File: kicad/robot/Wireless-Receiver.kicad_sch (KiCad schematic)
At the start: 49 parts, among them IC2 STWLC38JRM, J8 Conn_01x02

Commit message: Updated 100uF caps to 1206 footprint to allow for 6.3V ratings
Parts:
- C109, C125, C127, C131, C133, C135, C137, C138: footprint robot:C_0805_2012Metric -> robot:C_1206_3216Metric; Part Number (none) -> GRM31CD80J107MEA8K
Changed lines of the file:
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@@
       (effects (font (size 1.27 1.27)) (justify left))
     )
-    (property "Footprint" "robot:C_0805_2012Metric" (at 157.48 123.4948 0)
+    (property "Footprint" "robot:C_1206_3216Metric" (at 157.48 123.4948 0)
       (effects (font (size 1.27 1.27)) hide)
     )
@@
       (effects (font (size 1.27 1.27)) hide)
     )
-    (property "Part Number" "" (at 161.29 124.46 0)
+    (property "Part Number" "GRM31CD80J107MEA8K" (at 161.29 124.46 0)
       (effects (font (size 1.27 1.27)) hide)
     )
@@
       (effects (font (size 1.27 1.27)) (justify left))
     )
-    (property "Footprint" "robot:C_0805_2012Metric" (at 262.5852 116.84 0)
+    (property "Footprint" "robot:C_1206_3216Metric" (at 262.5852 116.84 0)
       (effects (font (size 1.27 1.27)) hide)
     )
@@
       (effects (font (size 1.27 1.27)) hide)
     )
-    (property "Part Number" "" (at 261.62 120.65 0)
+    (property "Part Number" "GRM31CD80J107MEA8K" (at 261.62 120.65 0)
       (effects (font (size 1.27 1.27)) hide)
     )
@@
       (effects (font (size 1.27 1.27)) (justify left))
     )
-    (property "Footprint" "robot:C_0805_2012Metric" (at 157.48 137.4648 0)
+    (property "Footprint" "robot:C_1206_3216Metric" (at 157.48 137.4648 0)
       (effects (font (size 1.27 1.27)) hide)
     )
@@
       (effects (font (size 1.27 1.27)) hide)
     )
-    (property "Part Number" "" (at 161.29 138.43 0)
+    (property "Part Number" "GRM31CD80J107MEA8K" (at 161.29 138.43 0)
       (effects (font (size 1.27 1.27)) hide)
     )
@@
       (effects (font (size 1.27 1.27)) (justify left))
     )
-    (property "Footprint" "robot:C_0805_2012Metric" (at 223.2152 144.78 0)
+    (property "Footprint" "robot:C_1206_3216Metric" (at 223.2152 144.78 0)
       (effects (font (size 1.27 1.27)) hide)
     )
@@
       (effects (font (size 1.27 1.27)) hide)
     )
-    (property "Part Number" "" (at 222.25 148.59 0)
+    (property "Part Number" "GRM31CD80J107MEA8K" (at 222.25 148.59 0)
       (effects (font (size 1.27 1.27)) hide)
     )
@@
       (effects (font (size 1.27 1.27)) (justify left))
     )
-    (property "Footprint" "robot:C_0805_2012Metric" (at 197.8152 144.78 0)
+    (property "Footprint" "robot:C_1206_3216Metric" (at 197.8152 144.78 0)
       (effects (font (size 1.27 1.27)) hide)
     )
@@
       (effects (font (size 1.27 1.27)) hide)
     )
-    (property "Part Number" "" (at 196.85 148.59 0)
+    (property "Part Number" "GRM31CD80J107MEA8K" (at 196.85 148.59 0)
       (effects (font (size 1.27 1.27)) hide)
     )
@@
       (effects (font (size 1.27 1.27)) (justify left))
     )
-    (property "Footprint" "robot:C_0805_2012Metric" (at 62.5348 125.73 0)
+    (property "Footprint" "robot:C_1206_3216Metric" (at 62.5348 125.73 0)
       (effects (font (size 1.27 1.27)) hide)
     )
@@
       (effects (font (size 1.27 1.27)) hide)
     )
-    (property "Part Number" "" (at 63.5 121.92 0)
+    (property "Part Number" "GRM31CD80J107MEA8K" (at 63.5 121.92 0)
       (effects (font (size 1.27 1.27)) hide)
     )
@@
       (effects (font (size 1.27 1.27)) (justify left))
     )
-    (property "Footprint" "robot:C_0805_2012Metric" (at 247.3452 116.84 0)
+    (property "Footprint" "robot:C_1206_3216Metric" (at 247.3452 116.84 0)
       (effects (font (size 1.27 1.27)) hide)
     )
@@
       (effects (font (size 1.27 1.27)) hide)
     )
-    (property "Part Number" "" (at 246.38 120.65 0)
+    (property "Part Number" "GRM31CD80J107MEA8K" (at 246.38 120.65 0)
       (effects (font (size 1.27 1.27)) hide)
     )
@@
       (effects (font (size 1.27 1.27)) (justify left))
     )
-    (property "Footprint" "robot:C_0805_2012Metric" (at 210.5152 144.78 0)
+    (property "Footprint" "robot:C_1206_3216Metric" (at 210.5152 144.78 0)
       (effects (font (size 1.27 1.27)) hide)
     )
@@
       (effects (font (size 1.27 1.27)) hide)
     )
-    (property "Part Number" "" (at 209.55 148.59 0)
-      (effects (font (size 1.27 1.27)) hide)
-    )
+    (property "Part Number" "GRM31CD80J107MEA8K" (at 209.55 148.59 0)
+      (effects (font (size 1.27 1.27)) hide)
+    )

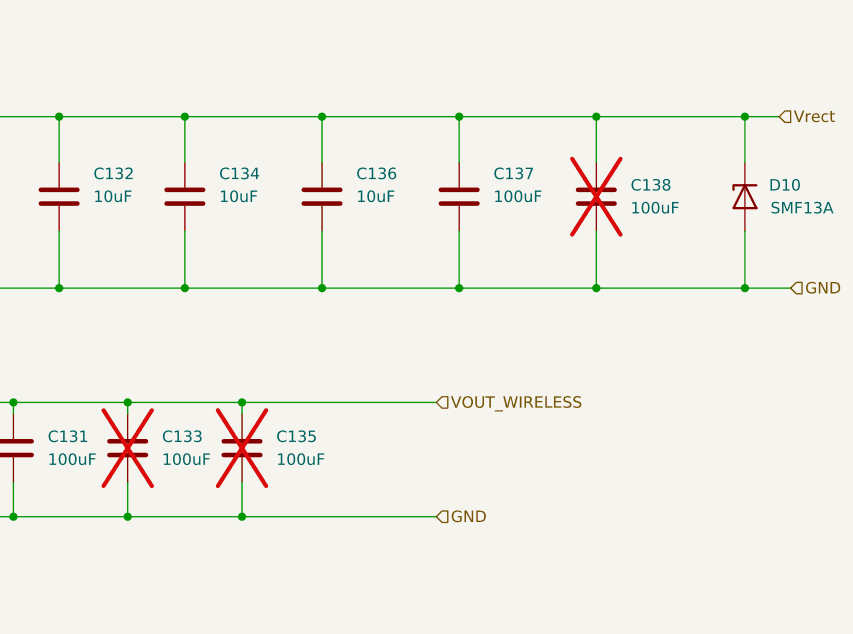
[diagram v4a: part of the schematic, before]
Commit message: Updating wireless 100uF caps to 16V 1210 versions
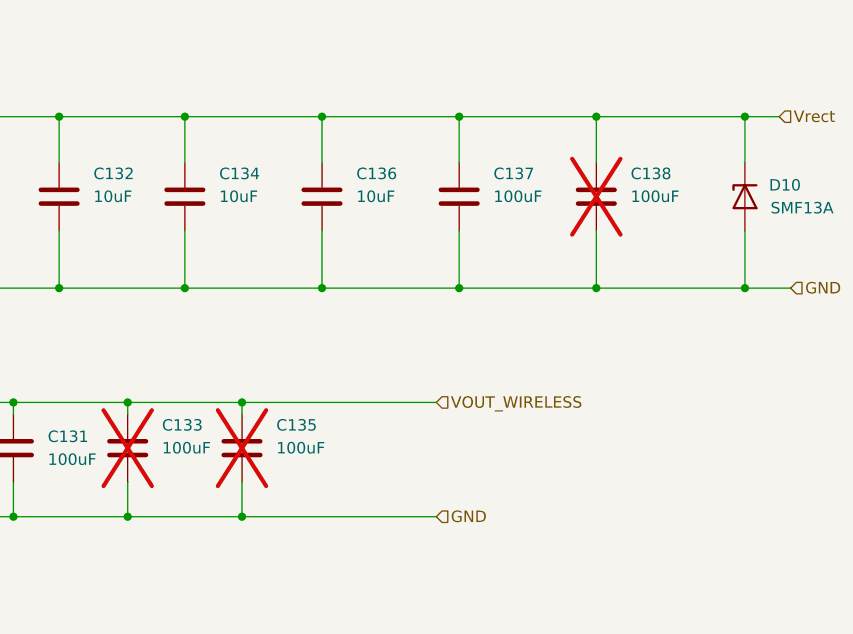
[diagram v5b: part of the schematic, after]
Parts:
- C133, C135, C137, C138: footprint robot:C_1206_3216Metric -> robot:C_1210_3225Metric; Manufacturer Murata -> Cal-Chip Electronics, Inc.; Part Number GRM31CD80J107MEA8K -> GMC32X5R107M16NT; V_Max (none) -> 16V
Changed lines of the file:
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@@
+    )
+  )
+  (symbol (lib_id "robot:C") (at 261.62 120.65 0) (mirror x) (unit 1)
+    (in_bom yes) (on_board yes) (dnp yes)
+    (property "Reference" "C138" (at 265.43 118.11 0)
+      (effects (font (size 1.27 1.27)) (justify left))
+    )
+    (property "Value" "100uF" (at 265.43 120.65 0)
+      (effects (font (size 1.27 1.27)) (justify left))
+    )
+    (property "Footprint" "robot:C_1210_3225Metric" (at 262.5852 116.84 0)
+      (effects (font (size 1.27 1.27)) hide)
+    )
+    (property "Datasheet" "~" (at 261.62 120.65 0)
+      (effects (font (size 1.27 1.27)) hide)
+    )
+    (property "Manufacturer" "Cal-Chip Electronics, Inc." (at 261.62 120.65 0)
+      (effects (font (size 1.27 1.27)) hide)
+    )
+    (property "Part Number" "GMC32X5R107M16NT" (at 261.62 120.65 0)
+      (effects (font (size 1.27 1.27)) hide)
+    )
+    (property "V_Max" "16V" (at 261.62 120.65 0)
+      (effects (font (size 1.27 1.27)) hide)
+    )
+    (pin "1")
+    (pin "2")
+    (instances
+      (project "robot"
+        (path "/0c7b298e-2d07-4b1f-b033-e95f02d45089/d5c9d5c0-7de4-474c-9ba2-6b466f104c70"
+          (reference "C138") (unit 1)
+        )
+      )
     )
   )
@@
     )
   )
-  (symbol (lib_id "robot:C") (at 261.62 120.65 0) (mirror x) (unit 1)
-    (in_bom yes) (on_board yes) (dnp yes)
-    (property "Reference" "C138" (at 265.43 119.38 0)
-      (effects (font (size 1.27 1.27)) (justify left))
-    )
-    (property "Value" "100uF" (at 265.43 121.92 0)
-      (effects (font (size 1.27 1.27)) (justify left))
-    )
-    (property "Footprint" "robot:C_1206_3216Metric" (at 262.5852 116.84 0)
-      (effects (font (size 1.27 1.27)) hide)
-    )
-    (property "Datasheet" "~" (at 261.62 120.65 0)
-      (effects (font (size 1.27 1.27)) hide)
-    )
-    (property "Manufacturer" "Murata" (at 261.62 120.65 0)
-      (effects (font (size 1.27 1.27)) hide)
-    )
-    (property "Part Number" "GRM31CD80J107MEA8K" (at 261.62 120.65 0)
-      (effects (font (size 1.27 1.27)) hide)
-    )
-    (pin "1")
-    (pin "2")
-    (instances
-      (project "robot"
-        (path "/0c7b298e-2d07-4b1f-b033-e95f02d45089/d5c9d5c0-7de4-474c-9ba2-6b466f104c70"
-          (reference "C138") (unit 1)
-        )
-      )
-    )
-  )
   (symbol (lib_id "robot:C") (at 129.54 49.53 90) (unit 1)
     (in_bom yes) (on_board yes) (dnp no)
@@
     )
   )
-  (symbol (lib_id "robot:C") (at 222.25 148.59 0) (mirror x) (unit 1)
+  (symbol (lib_id "robot:C") (at 209.55 148.59 0) (mirror x) (unit 1)
     (in_bom yes) (on_board yes) (dnp yes)
-    (property "Reference" "C135" (at 226.06 147.32 0)
-      (effects (font (size 1.27 1.27)) (justify left))
-    )
-    (property "Value" "100uF" (at 226.06 149.86 0)
-      (effects (font (size 1.27 1.27)) (justify left))
-    )
-    (property "Footprint" "robot:C_1206_3216Metric" (at 223.2152 144.78 0)
-      (effects (font (size 1.27 1.27)) hide)
-    )
-    (property "Datasheet" "~" (at 222.25 148.59 0)
-      (effects (font (size 1.27 1.27)) hide)
-    )
-    (property "Manufacturer" "Murata" (at 222.25 148.59 0)
-      (effects (font (size 1.27 1.27)) hide)
-    )
-    (property "Part Number" "GRM31CD80J107MEA8K" (at 222.25 148.59 0)
-      (effects (font (size 1.27 1.27)) hide)
-    )
-    (pin "1")
-    (pin "2")
-    (instances
-      (project "robot"
-        (path "/0c7b298e-2d07-4b1f-b033-e95f02d45089/d5c9d5c0-7de4-474c-9ba2-6b466f104c70"
-          (reference "C135") (unit 1)
+    (property "Reference" "C133" (at 213.36 146.05 0)
+      (effects (font (size 1.27 1.27)) (justify left))
+    )
+    (property "Value" "100uF" (at 213.36 148.59 0)
+      (effects (font (size 1.27 1.27)) (justify left))
+    )
+    (property "Footprint" "robot:C_1210_3225Metric" (at 210.5152 144.78 0)
+      (effects (font (size 1.27 1.27)) hide)
+    )
+    (property "Datasheet" "~" (at 209.55 148.59 0)
+      (effects (font (size 1.27 1.27)) hide)
+    )
+    (property "Manufacturer" "Cal-Chip Electronics, Inc." (at 209.55 148.59 0)
+      (effects (font (size 1.27 1.27)) hide)
+    )
+    (property "Part Number" "GMC32X5R107M16NT" (at 209.55 148.59 0)
+      (effects (font (size 1.27 1.27)) hide)
+    )
+    (property "V_Max" "16V" (at 209.55 148.59 0)
+      (effects (font (size 1.27 1.27)) hide)
+    )
+    (pin "1")
+    (pin "2")
+    (instances
+      (project "robot"
+        (path "/0c7b298e-2d07-4b1f-b033-e95f02d45089/d5c9d5c0-7de4-474c-9ba2-6b466f104c70"
+          (reference "C133") (unit 1)
         )
       )
@@
     )
   )
+  (symbol (lib_id "robot:C") (at 222.25 148.59 0) (mirror x) (unit 1)
+    (in_bom yes) (on_board yes) (dnp yes)
+    (property "Reference" "C135" (at 226.06 146.05 0)
+      (effects (font (size 1.27 1.27)) (justify left))
+    )
+    (property "Value" "100uF" (at 226.06 148.59 0)
+      (effects (font (size 1.27 1.27)) (justify left))
+    )
+    (property "Footprint" "robot:C_1210_3225Metric" (at 223.2152 144.78 0)
+      (effects (font (size 1.27 1.27)) hide)
+    )
+    (property "Datasheet" "~" (at 222.25 148.59 0)
+      (effects (font (size 1.27 1.27)) hide)
+    )
+    (property "Manufacturer" "Cal-Chip Electronics, Inc." (at 222.25 148.59 0)
+      (effects (font (size 1.27 1.27)) hide)
+    )
+    (property "Part Number" "GMC32X5R107M16NT" (at 222.25 148.59 0)
+      (effects (font (size 1.27 1.27)) hide)
+    )
+    (property "V_Max" "16V" (at 222.25 148.59 0)
+      (effects (font (size 1.27 1.27)) hide)
+    )
+    (pin "1")
+    (pin "2")
+    (instances
+      (project "robot"
+        (path "/0c7b298e-2d07-4b1f-b033-e95f02d45089/d5c9d5c0-7de4-474c-9ba2-6b466f104c70"
+          (reference "C135") (unit 1)
+        )
+      )
+    )
+  )
   (symbol (lib_id "robot:C") (at 246.38 120.65 0) (mirror x) (unit 1)
     (in_bom yes) (on_board yes) (dnp no)
@@
       (effects (font (size 1.27 1.27)) (justify left))
     )
-    (property "Footprint" "robot:C_1206_3216Metric" (at 247.3452 116.84 0)
+    (property "Footprint" "robot:C_1210_3225Metric" (at 247.3452 116.84 0)
       (effects (font (size 1.27 1.27)) hide)
     )
@@
       (effects (font (size 1.27 1.27)) hide)
     )
-    (property "Manufacturer" "Murata" (at 246.38 120.65 0)
-      (effects (font (size 1.27 1.27)) hide)
-    )
-    (property "Part Number" "GRM31CD80J107MEA8K" (at 246.38 120.65 0)
+    (property "Manufacturer" "Cal-Chip Electronics, Inc." (at 246.38 120.65 0)
+      (effects (font (size 1.27 1.27)) hide)
+    )
+    (property "Part Number" "GMC32X5R107M16NT" (at 246.38 120.65 0)
+      (effects (font (size 1.27 1.27)) hide)
+    )
+    (property "V_Max" "16V" (at 246.38 120.65 0)
       (effects (font (size 1.27 1.27)) hide)
     )
@@
         )
       )
-    )
-  )
-  (symbol (lib_id "robot:C") (at 209.55 148.59 0) (mirror x) (unit 1)
-    (in_bom yes) (on_board yes) (dnp yes)
-    (property "Reference" "C133" (at 213.36 147.32 0)
-      (effects (font (size 1.27 1.27)) (justify left))
-    )
-    (property "Value" "100uF" (at 213.36 149.86 0)
-      (effects (font (size 1.27 1.27)) (justify left))
-    )
-    (property "Footprint" "robot:C_1206_3216Metric" (at 210.5152 144.78 0)
-      (effects (font (size 1.27 1.27)) hide)
-    )
-    (property "Datasheet" "~" (at 209.55 148.59 0)
-      (effects (font (size 1.27 1.27)) hide)
-    )
-    (property "Manufacturer" "Murata" (at 209.55 148.59 0)
-      (effects (font (size 1.27 1.27)) hide)
-    )
-    (property "Part Number" "GRM31CD80J107MEA8K" (at 209.55 148.59 0)
-      (effects (font (size 1.27 1.27)) hide)
-    )
-    (pin "1")
-    (pin "2")
-    (instances
-      (project "robot"
-        (path "/0c7b298e-2d07-4b1f-b033-e95f02d45089/d5c9d5c0-7de4-474c-9ba2-6b466f104c70"
-          (reference "C133") (unit 1)
-        )
-      )

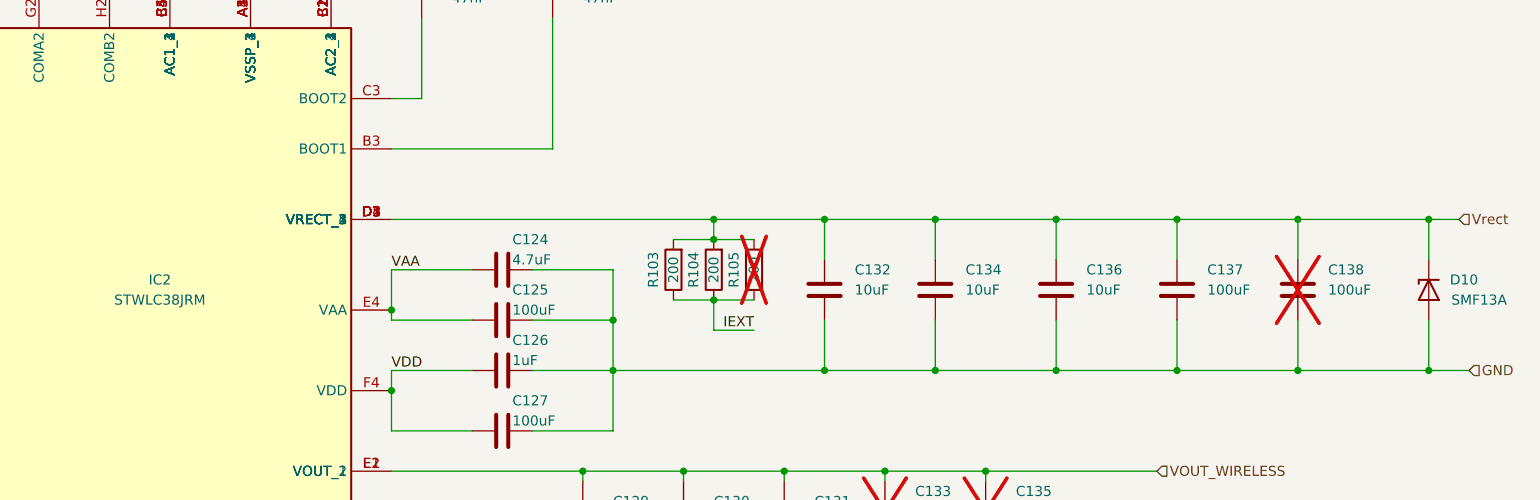
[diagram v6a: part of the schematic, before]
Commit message: Adding wireless charger circuit
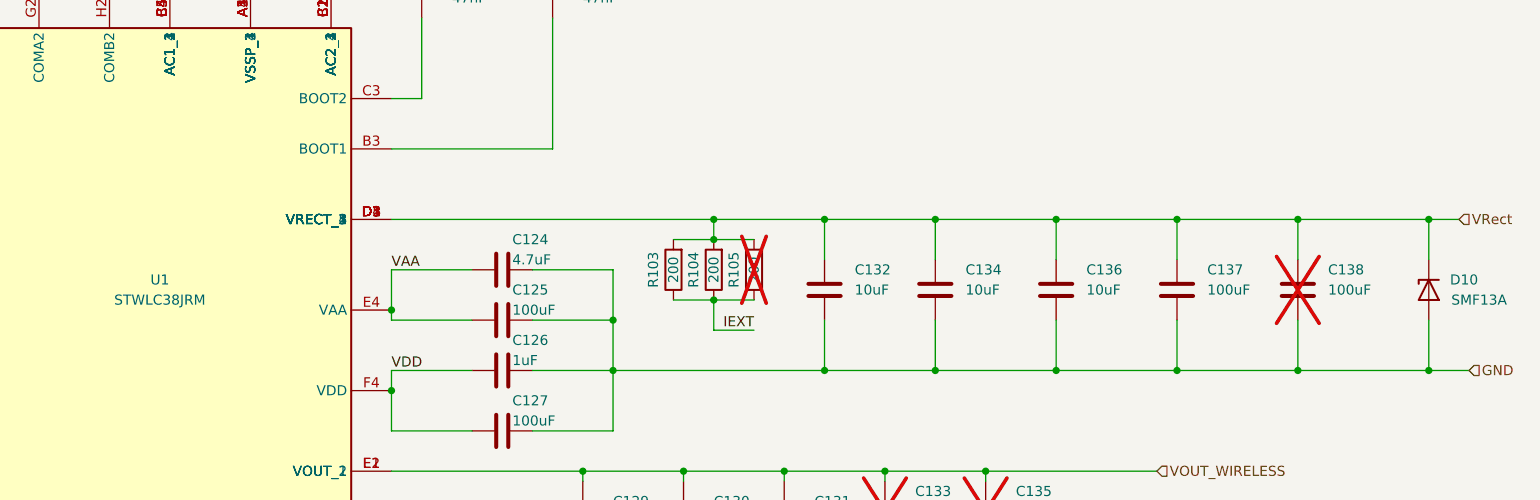
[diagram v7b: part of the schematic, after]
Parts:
- C131: footprint robot:C_1206_3216Metric -> robot:C_1210_3225Metric
- renumbered IC2 to U1
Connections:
- net Vrect renamed VRect
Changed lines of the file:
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@@
     (effects (font (size 1.27 1.27)) (justify left))
   )
-  (hierarchical_label "Vrect" (shape input) (at 281.94 111.76 0) (fields_autoplaced)
+  (hierarchical_label "VRect" (shape input) (at 281.94 111.76 0) (fields_autoplaced)
     (effects (font (size 1.27 1.27)) (justify left))
   )
@@
   (symbol (lib_id "robot:STWLC38JRM") (at 118.11 120.65 0) (unit 1)
     (in_bom yes) (on_board yes) (dnp no)
-    (property "Reference" "IC2" (at 118.11 119.38 0)
+    (property "Reference" "U1" (at 118.11 119.38 0)
       (effects (font (size 1.27 1.27)))
     )
@@
       (project "robot"
         (path "/0c7b298e-2d07-4b1f-b033-e95f02d45089/d5c9d5c0-7de4-474c-9ba2-6b466f104c70"
-          (reference "IC2") (unit 1)
+          (reference "U1") (unit 1)
         )
       )
@@
       (effects (font (size 1.27 1.27)) (justify left))
     )
-    (property "Footprint" "robot:C_1206_3216Metric" (at 197.8152 144.78 0)
+    (property "Footprint" "robot:C_1210_3225Metric" (at 197.8152 144.78 0)
       (effects (font (size 1.27 1.27)) hide)
     )
@@
   )
   (symbol (lib_id "robot:INDUCTOR") (at 129.54 33.02 0) (unit 1)
-    (in_bom yes) (on_board yes) (dnp yes)
+    (in_bom yes) (on_board no) (dnp yes)
     (property "Reference" "L5" (at 129.54 29.21 0)
       (effects (font (size 1.27 1.27)))

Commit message: fixed two wrong product foorprint mismatches
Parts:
- C111: footprint robot:C_0603_1608Metric -> robot:C_0402_1005Metric
- R101: footprint robot:R_0603_1608Metric -> robot:R_0402_1005Metric
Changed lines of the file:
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@@
       (effects (font (size 1.27 1.27)) (justify left))
     )
-    (property "Footprint" "robot:C_0603_1608Metric" (at 16.8148 101.6 0)
+    (property "Footprint" "robot:C_0402_1005Metric" (at 16.8148 101.6 0)
       (effects (font (size 1.27 1.27)) hide)
     )
@@
       (effects (font (size 1.27 1.27)))
     )
-    (property "Footprint" "robot:R_0603_1608Metric" (at 46.99 31.242 90)
-      (effects (font (size 1.27 1.27)) hide)
-    )
+    (property "Footprint" "robot:R_0402_1005Metric" (at 46.99 31.242 90)
+      (effects (font (size 1.27 1.27)) hide)
+    )
